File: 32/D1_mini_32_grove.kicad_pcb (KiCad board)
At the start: 2 copper layers, 31.6 x 37 mm, 10 parts, among them J1 Conn_01x04_Pin, J2 Conn_01x04_Pin, J3 Conn_01x04_Pin, J4 Conn_01x04_Pin, J5 Conn_01x04_Pin, SW1 SW_Wuerth_450301014042, U1 e

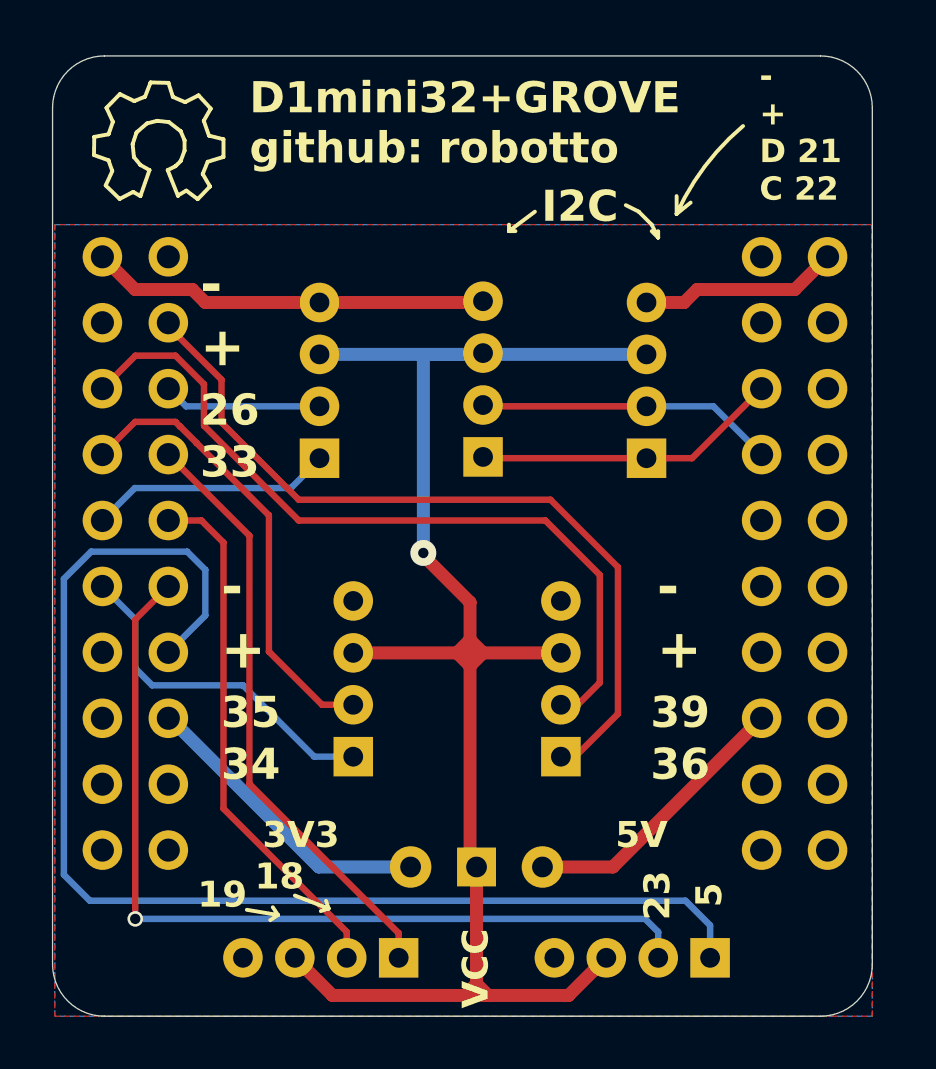
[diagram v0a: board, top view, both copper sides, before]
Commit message: Slighly modified layout for 3rd production run
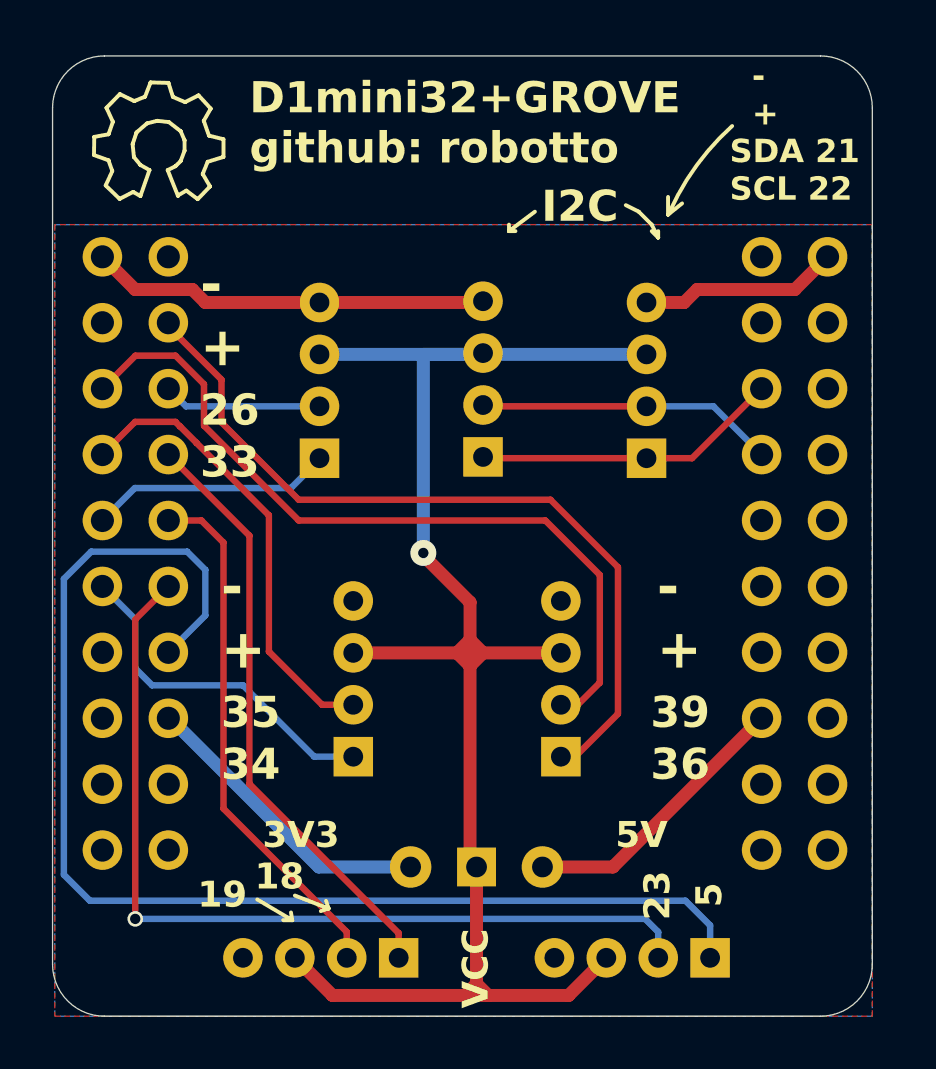
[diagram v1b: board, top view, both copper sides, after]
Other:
- board text added: "- + SDA 21 SCL 22"
- board text removed: "- + D 21 C 22"
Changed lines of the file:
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@@
 	)
 	(gr_line
-		(start 105.6 78.1)
-		(end 105.4 77.8)
+		(start 106.15 78.3)
+		(end 106.1 78)
 		(stroke
 			(width 0.15)
@@
 	)
 	(gr_line
-		(start 120.958777 51.086473)
-		(end 121.5 50.65)
+		(start 120.629388 51.118236)
+		(end 121.170611 50.681763)
 		(stroke
 			(width 0.15)
@@
 	)
 	(gr_line
-		(start 104.4 77.9)
-		(end 105.6 78.1)
-		(stroke
-			(width 0.15)
-			(type default)
-		)
-		(layer "F.SilkS")
-	)
-	(gr_arc
-		(start 120.958777 51.086471)
-		(mid 122.05 49.25)
-		(end 123.519756 47.699771)
-		(stroke
-			(width 0.15)
-			(type default)
-		)
-		(layer "F.SilkS")
-	)
-	(gr_line
-		(start 105.6 78.1)
-		(end 105.3 78.3)
+		(start 104.8 77.5)
+		(end 106.15 78.3)
+		(stroke
+			(width 0.15)
+			(type default)
+		)
+		(layer "F.SilkS")
+	)
+	(gr_arc
+		(start 120.707446 50.972773)
+		(mid 121.734238 49.212379)
+		(end 123.1 47.699771)
+		(stroke
+			(width 0.15)
+			(type default)
+		)
+		(layer "F.SilkS")
+	)
+	(gr_line
+		(start 106.15 78.3)
+		(end 105.8 78.3)
 		(stroke
 			(width 0.15)
@@
 	)
 	(gr_line
-		(start 120.958777 51.086473)
-		(end 120.958777 50.4)
+		(start 120.629388 51.118236)
+		(end 120.629388 50.431763)
 		(stroke
 			(width 0.15)
@@
 		)
 	)
-	(gr_text "-\n+\nD 21\nC 22"
-		(at 124.15 50.65 0)
-		(layer "F.SilkS")
-		(effects
+	(gr_text "  -\n  +\nSDA 21\nSCL 22"
+		(at 123 50.65 0)
+		(layer "F.SilkS")
+		(effects

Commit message: Added silkscreen info about input only pins
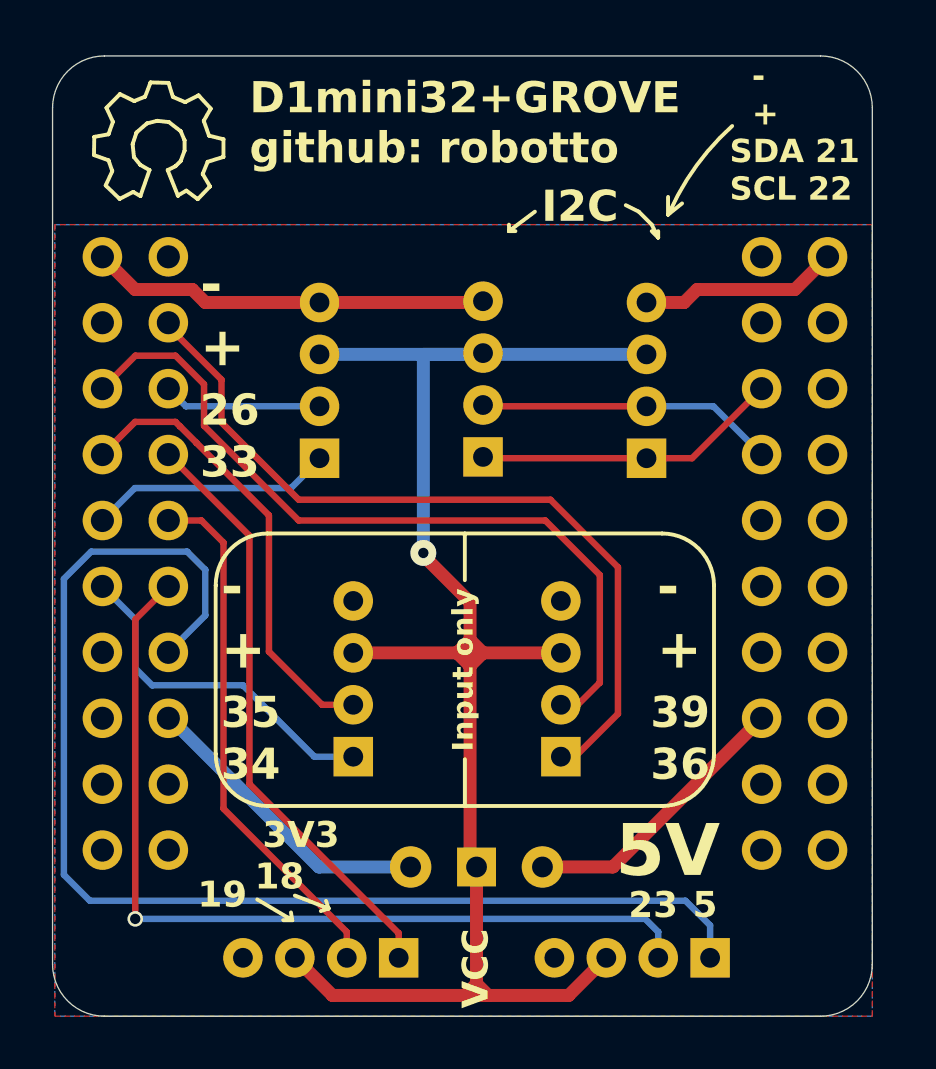
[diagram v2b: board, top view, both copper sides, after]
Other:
- board text added: "Input only"
